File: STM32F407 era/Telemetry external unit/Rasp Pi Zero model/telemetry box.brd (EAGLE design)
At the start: 160 x 100 mm, 53 parts, among them IC1 MCP73831/OT, IC2 MCP73831/OT, IC3 MCP73831/OT, IC4 74AC14D, IC5 74HC08D, IC6 74AC32D, IC7 317T, IC8 MCP3202SN, U1 SC18IM700IPW,112

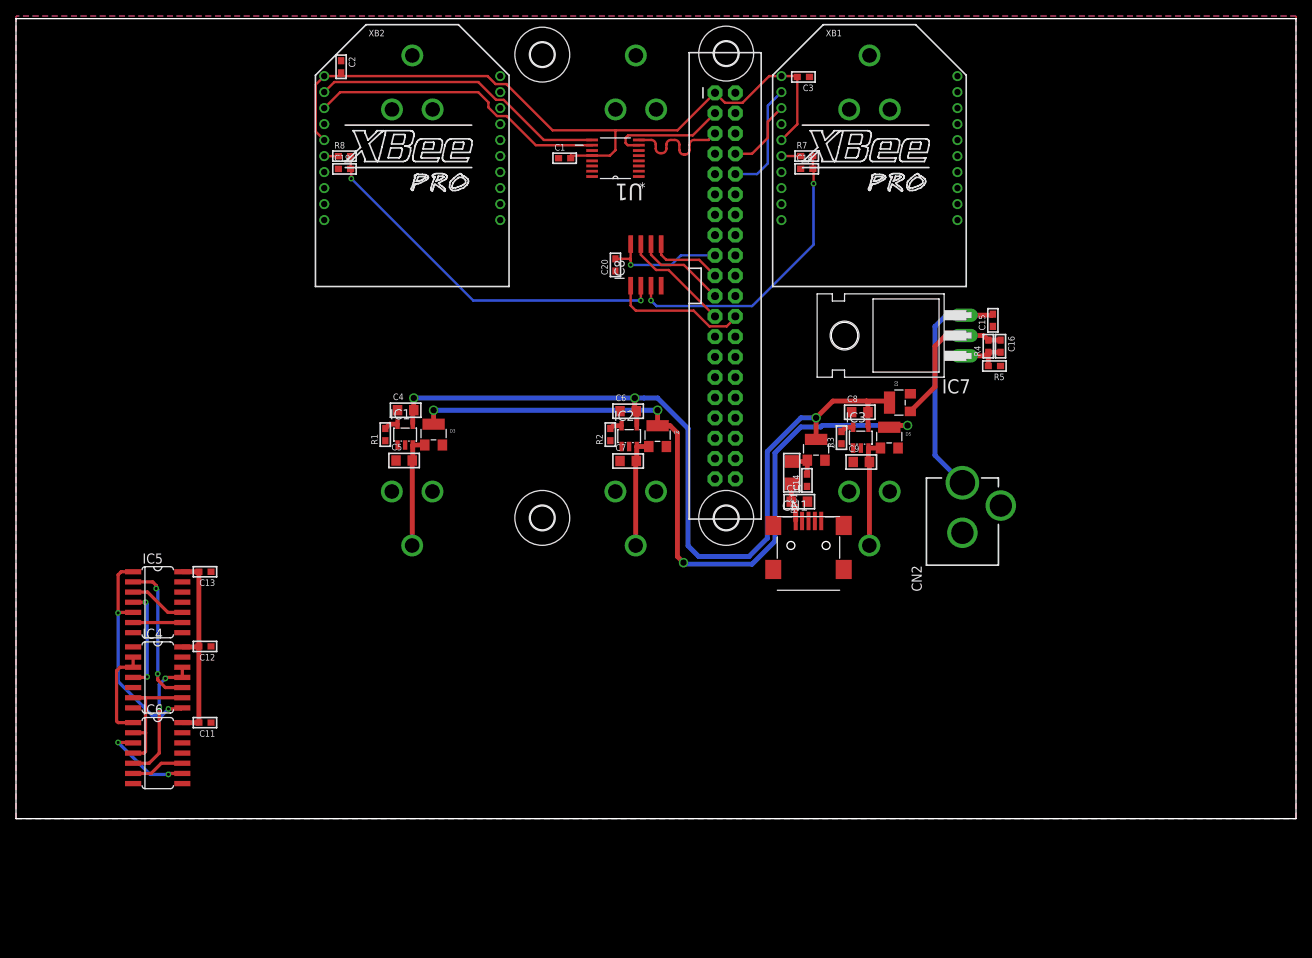
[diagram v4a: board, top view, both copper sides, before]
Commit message: added 5V boost circuit for tele unit
also should be done now
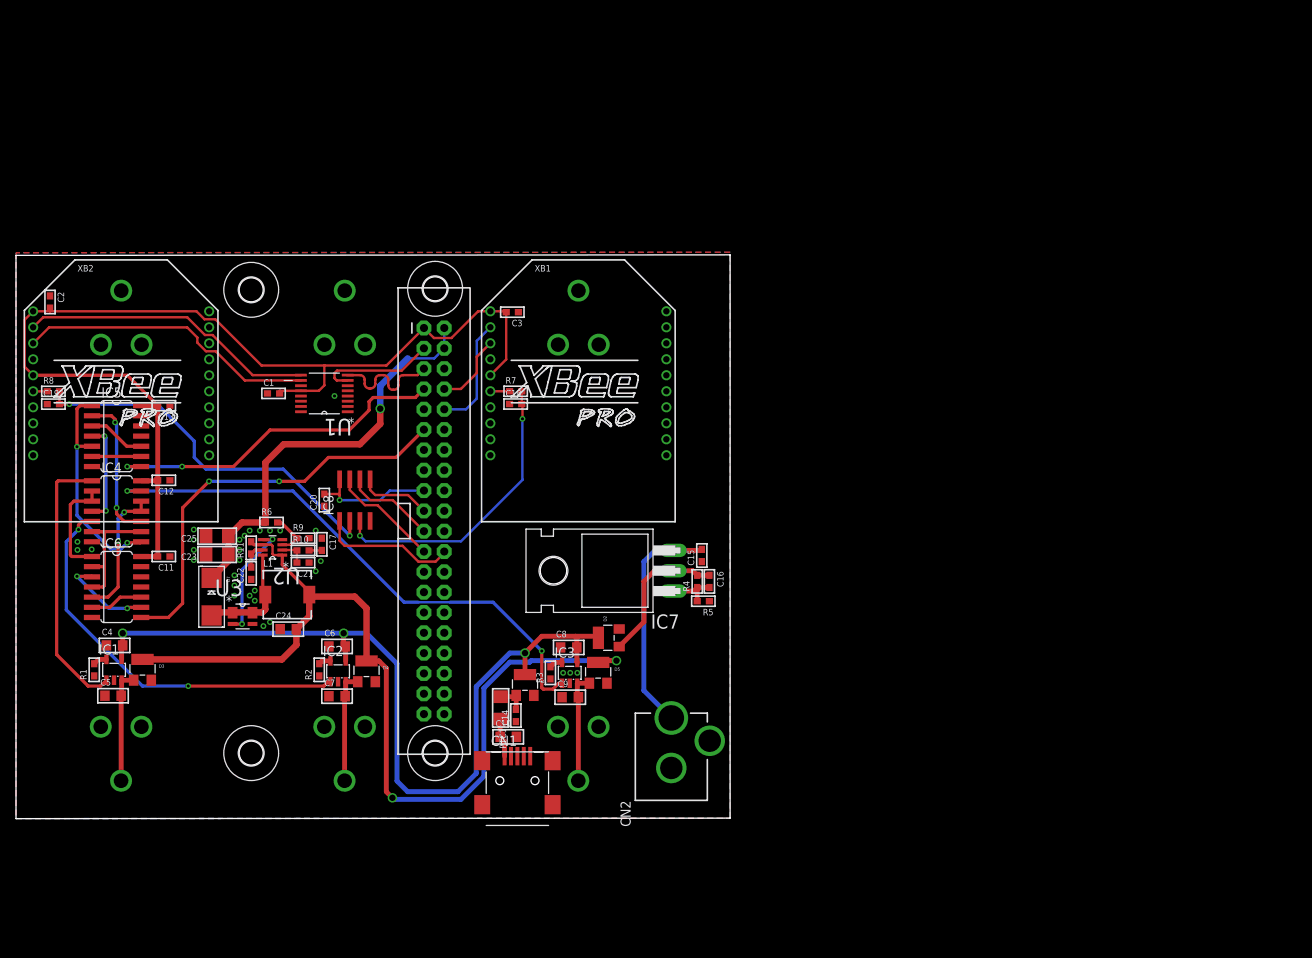
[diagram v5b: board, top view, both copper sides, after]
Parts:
- added C17: 1n8, microbuilder:_0603
- added C21: 47p, microbuilder:_0603
- added C22: 1n, microbuilder:_0603
- added C23, C25: 100u, microbuilder:1206
- added C24: 10u, microbuilder:_0805
- added D7: B320, adafruit:SMADIODE
- added L1: FDVE0630-H-1R0M, microbuilder:INDUCTOR_6X6MM_TDK_SLF6045
- added R10: 17k4, microbuilder:_0603
- added R11: 1m, microbuilder:_0603
- added R6: 34k8, microbuilder:_0603
- added R9: 11k, microbuilder:_0603
- added U2: LTC3872ETS8TRMPBF, LTC_By_element14_Batch_1:SOT65P280X100-8N
- added U3: SI3460DDV-T1-GE3, Vishay_By_element14_Batch_1:SOT95P285X110-6N
- moved C15 46.8 mm to (85.7, 32.9)
- moved C16 46.8 mm to (86.7, 29.7)
- moved C18 46.8 mm to (62.5, 51.8)
- moved C2 46.8 mm to (4.25, 64.6)
- moved C20 46.8 mm to (38.5, 39.8)
- moved C8 46.8 mm to (69.1, 21.4)
- moved C9 46.8 mm to (69.3, 15.2)
- moved D4 46.8 mm to (43.8, 18.4)
- moved H2 46.8 mm to (29.4, 66.1)
- moved R4 46.8 mm to (85.2, 29.7)
- moved R5 46.8 mm to (85.9, 27.2)
- moved BAT1 46.8 mm to (13.1, 35.4)
- moved BAT2 46.8 mm to (41.1, 35.4)
- moved BAT3 46.8 mm to (70.3, 35.4)
- moved C1 46.8 mm to (32.2, 53.1)
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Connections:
- new net CHARGE-DONE: IC5.8, JP1.7
- new net CHARGING: IC6.8, JP1.11
- new net MOSD: D7.A, L1.P$1, U2.8, U3.1, U3.2, U3.5, U3.6
- new net N$19: R6.2, R9.1, U2.3
- new net N$25: U2.5, U3.3
- new net N$26: C17.2, R10.2
- new net N$27: C21.2, R10.1, U2.2
- new net N$29: C22.2, R11.1, U2.7
- net 5.0V: now also C23.1, C25.1, D7.C, R6.1
- net GND: now also C17.1, C21.1, C22.1, C23.2, C24.1, C25.2, R9.2, U2.4, U3.4
- net VBAT: now also C24.2, L1.P$2, R11.2, U2.1, U2.6
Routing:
- net BAT-STAT3: track 0.00 -> 69.3 mm, vias 0 -> 2
- net 5.0V: track 0.00 -> 52.5 mm, vias 0 -> 1
- net CHARGING: track 0.00 -> 52.1 mm, vias 0 -> 2
- net BAT-STAT2: track 0.00 -> 50.3 mm, vias 0 -> 2
- net CHARGE-DONE: track 0.00 -> 43.5 mm, vias 0 -> 2
- net BAT-STAT1: track 0.00 -> 34.2 mm
- net VBAT: track 95.3 -> 116.4 mm, vias 4 -> 2
- net 3.3V: track 133.2 -> 150.3 mm
- net MOSD: track 0.00 -> 16.6 mm
- net N$25: track 0.00 -> 14.6 mm, vias 0 -> 2
- net N$19: track 0.00 -> 5.39 mm
- net N$27: track 0.00 -> 3.37 mm
- net N$29: track 0.00 -> 3.30 mm
- net N$26: track 0.00 -> 1.59 mm
- net N$11: track 12.0 -> 13.2 mm
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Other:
- board size 160 x 100 mm -> 89.3 x 70.5 mm

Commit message: more final board prepping for production
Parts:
- removed C1: 100n, microbuilder:_0603
- removed U1: SC18IM700IPW,112, NXP_By_element14_Batch_1:SOP65P640X110-16N
- added C26: 100n, microbuilder:_0603
- added U4: SC16IS740IPW,112, NXP-SC16IS740IPW-112:SOP65P640X110-16N
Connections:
- net 3.3V: now also C26.2, U4.1, U4.8; no longer C1.2, U1.12
- net GND: now also C26.1, U4.2, U4.3, U4.9; no longer C1.1, U1.4
- net LAP-RX: now also U4.13; no longer U1.9
- net LAP-TX: now also U4.12; no longer U1.10
- net SCL: now also U4.5; no longer U1.8
- net SDA: now also U4.6; no longer U1.7
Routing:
- net SDA: track 15.1 -> 12.6 mm
- net SCL: track 14.1 -> 11.8 mm
- net 3.3V: track 150.3 -> 152.5 mm
- net LAP-RX: track 37.0 -> 37.3 mm, vias 0 -> 2

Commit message: change in power circuit
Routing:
- net 3.3V: track 152.5 -> 154.9 mm, vias 1 -> 0
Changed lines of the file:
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@@
 <contactref element="IC8" pad="8"/>
 <contactref element="C20" pad="2"/>
-<wire x1="50.9905" y1="41.0083" x2="46.7233" y2="41.0083" width="0.3048" layer="16"/>
-<wire x1="46.7233" y1="41.0083" x2="45.5295" y2="39.8145" width="0.3048" layer="16"/>
-<wire x1="45.5295" y1="39.8145" x2="40.4495" y2="39.8145" width="0.3048" layer="16"/>
-<via x="40.4495" y="39.8145" extent="1-16" drill="0.381"/>
-<wire x1="40.4495" y1="39.8145" x2="40.4495" y2="40.4495" width="0.3048" layer="1"/>
-<wire x1="40.4495" y1="40.4495" x2="40.4495" y2="42.4145" width="0.3048" layer="1"/>
-<wire x1="38.5445" y1="40.5765" x2="40.3225" y2="40.5765" width="0.3048" layer="1"/>
-<wire x1="40.3225" y1="40.5765" x2="40.4495" y2="40.4495" width="0.3048" layer="1"/>
 <wire x1="59.2945" y1="55.4195" x2="61.2775" y2="57.4025" width="0.3048" layer="1"/>
 <wire x1="61.2775" y1="57.4025" x2="61.2775" y2="63.3095" width="0.3048" layer="1"/>
@@
 <contactref element="U4" pad="8"/>
 <wire x1="38.227" y1="49.8475" x2="38.227" y2="51.054" width="0.3048" layer="1"/>
-<wire x1="38.227" y1="51.1175" x2="38.227" y2="55.626" width="0.3048" layer="1"/>
+<wire x1="38.227" y1="51.054" x2="38.227" y2="55.626" width="0.3048" layer="1"/>
 <wire x1="38.227" y1="55.626" x2="38.227" y2="56.642" width="0.3048" layer="1"/>
 <wire x1="40.259" y1="55.626" x2="38.227" y2="55.626" width="0.3048" layer="1"/>
 <wire x1="40.259" y1="51.054" x2="38.227" y2="51.054" width="0.3048" layer="1"/>
-<wire x1="38.227" y1="51.054" x2="38.227" y2="51.1175" width="0.3048" layer="1"/>
-<wire x1="38.227" y1="49.8475" x2="40.4495" y2="42.4145" width="0" layer="19" extent="1-1"/>
+<wire x1="38.5445" y1="40.5765" x2="39.9415" y2="40.5765" width="0.3048" layer="1"/>
+<wire x1="39.9415" y1="40.5765" x2="40.4495" y2="41.0845" width="0.3048" layer="1"/>
+<wire x1="40.4495" y1="41.0845" x2="40.4495" y2="41.91" width="0.3048" layer="1"/>
+<wire x1="40.4495" y1="41.91" x2="40.4495" y2="42.4145" width="0.3048" layer="1"/>
+<wire x1="50.9905" y1="41.0083" x2="45.6692" y2="41.0083" width="0.3048" layer="1"/>
+<wire x1="45.6692" y1="41.0083" x2="45.085" y2="41.5925" width="0.3048" layer="1"/>
+<wire x1="45.085" y1="41.5925" x2="45.085" y2="43.815" width="0.3048" layer="1"/>
+<wire x1="45.085" y1="43.815" x2="44.7675" y2="44.1325" width="0.3048" layer="1"/>
+<wire x1="44.7675" y1="44.1325" x2="40.9575" y2="44.1325" width="0.3048" layer="1"/>
+<wire x1="40.9575" y1="44.1325" x2="40.4495" y2="43.6245" width="0.3048" layer="1"/>
+<wire x1="40.4495" y1="43.6245" x2="40.4495" y2="42.4145" width="0.3048" layer="1"/>
+<wire x1="38.227" y1="49.8475" x2="40.9575" y2="44.1325" width="0" layer="19" extent="1-1"/>
 </signal>
 <signal name="GND">
